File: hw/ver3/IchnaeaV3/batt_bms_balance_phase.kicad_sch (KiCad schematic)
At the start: 2 parts, among them Q31 Q_Dual_NMOS_S1G1D2S2G2D1

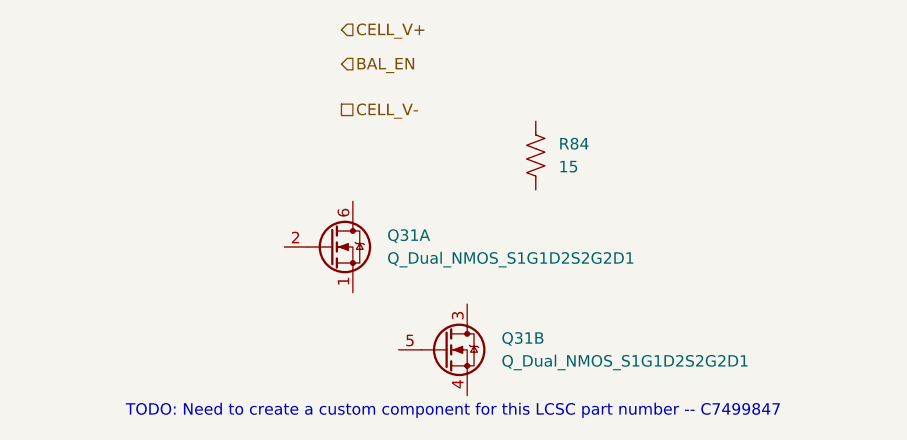
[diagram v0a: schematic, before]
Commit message: Experiment with a new power stage layout
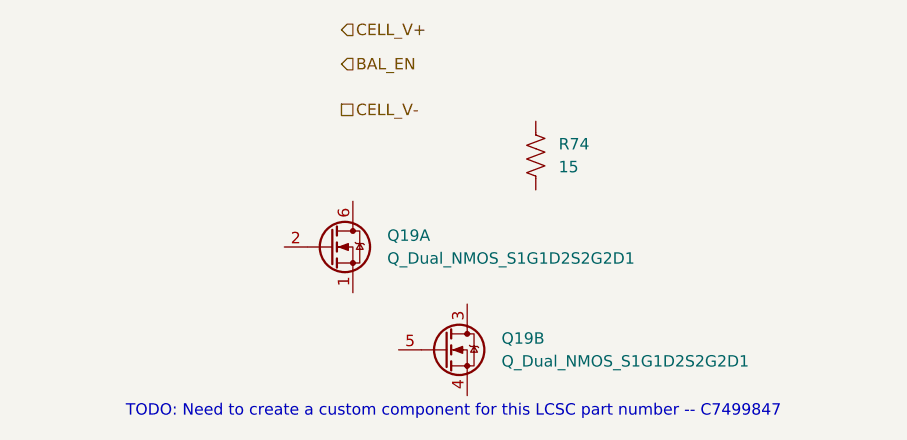
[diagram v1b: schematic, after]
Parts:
- renumbered Q31 to Q19, R84 to R74
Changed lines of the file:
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@@
 		(dnp no)
 		(fields_autoplaced yes)
-		(property "Reference" "R84"
+		(property "Reference" "R74"
 			(at 120.65 106.6799 0)
 			(effects
@@
 			(project "IchnaeaV3"
 				(path "/93408532-1ffa-463d-873c-16289d2b7987/f8cdf9d7-add1-4ff8-8430-918a71e3d1f9/15949d39-4147-469d-a992-c4b48798ba19/5d638572-1b20-446a-b8ff-9a7be673240d"
-					(reference "R84")
+					(reference "R74")
 					(unit 1)
 				)
@@
 		(dnp no)
 		(fields_autoplaced yes)
-		(property "Reference" "Q31"
+		(property "Reference" "Q19"
 			(at 114.3 128.2699 0)
 			(effects
@@
 			(project "IchnaeaV3"
 				(path "/93408532-1ffa-463d-873c-16289d2b7987/f8cdf9d7-add1-4ff8-8430-918a71e3d1f9/15949d39-4147-469d-a992-c4b48798ba19/5d638572-1b20-446a-b8ff-9a7be673240d"
-					(reference "Q31")
+					(reference "Q19")
 					(unit 2)
 				)
@@
 		(dnp no)
 		(fields_autoplaced yes)
-		(property "Reference" "Q31"
+		(property "Reference" "Q19"
 			(at 101.6 116.8399 0)
 			(effects
@@
 			(project "IchnaeaV3"
 				(path "/93408532-1ffa-463d-873c-16289d2b7987/f8cdf9d7-add1-4ff8-8430-918a71e3d1f9/15949d39-4147-469d-a992-c4b48798ba19/5d638572-1b20-446a-b8ff-9a7be673240d"
-					(reference "Q31")
+					(reference "Q19")
 					(unit 1)
 				)

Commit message: I might've made a critical error
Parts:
- R74: LCSC C2934051 -> C2934051
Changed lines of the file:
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@@
 			)
 		)
-		(property "LCSC" " C2934051"
+		(property "LCSC" "C2934051"
+			(at 118.11 107.95 0)
+			(effects
+				(font
+					(size 1.27 1.27)
+				)
+				(hide yes)
+			)
+		)
+		(property "JLCPCB Rotation Offset" ""
 			(at 118.11 107.95 0)
 			(effects
@@
 		)
 		(property "Description" "Dual NMOS transistor, 6 pin package"
+			(at 107.95 129.54 0)
+			(effects
+				(font
+					(size 1.27 1.27)
+				)
+				(hide yes)
+			)
+		)
+		(property "JLCPCB Rotation Offset" ""
 			(at 107.95 129.54 0)
 			(effects
@@
 			(at 95.25 118.11 0)
 			(effects
+				(font
+					(size 1.27 1.27)
+				)
+				(hide yes)
+			)
+		)
+		(property "JLCPCB Rotation Offset" ""
+			(at 95.25 118.11 0)
+			(effects
